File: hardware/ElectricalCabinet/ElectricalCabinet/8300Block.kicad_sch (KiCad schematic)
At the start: 0 parts

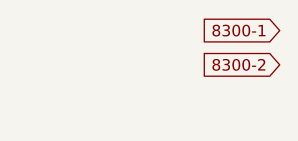
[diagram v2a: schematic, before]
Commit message: Further wiring updates
Populated 6100 Bus
Corrected number of relay boards
Added 110v outputs to relay boards and noted light positon
Uploaded light scheme to documents folder
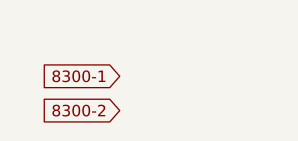
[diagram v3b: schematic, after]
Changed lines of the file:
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@@
 	(generator "eeschema")
 	(generator_version "10.0")
-	(paper "A4")
+	(paper "USLetter")
 	(global_label "8300-2"
 		(shape input)
-		(at 53.34 10.16 180)
+		(at 35.56 15.24 180)
 		(effects
 			(font
@@
 		)
 		(property "Intersheetrefs" "${INTERSHEET_REFS}"
-			(at 42.7349 10.16 0)
+			(at 24.9549 15.24 0)
 			(hide yes)
 			(show_name no)
@@
 		)
 		(property "Field" "5V Clock"
-			(at 44.45 10.16 0)
+			(at 26.67 15.24 0)
 			(hide yes)
 			(show_name no)
@@
 		)
 		(property "Ref" "Ref 333"
-			(at 43.18 10.16 0)
+			(at 25.4 15.24 0)
 			(show_name no)
 			(do_not_autoplace no)
@@
 	(global_label "8300-1"
 		(shape input)
-		(at 53.34 6.35 180)
+		(at 35.56 11.43 180)
 		(effects
 			(font
@@
 		)
 		(property "Intersheetrefs" "213"
-			(at 42.7349 6.35 0)
+			(at 24.9549 11.43 0)
 			(hide yes)
 			(show_name no)
@@
 		)
 		(property "Field" "5V Clock"
-			(at 44.45 6.35 0)
+			(at 26.67 11.43 0)
 			(hide yes)
 			(show_name no)
@@
 		)
 		(property "Ref" "Ref 213"
-			(at 43.18 6.35 0)
+			(at 25.4 11.43 0)
 			(show_name no)
 			(do_not_autoplace no)

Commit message: Electrical Cabinet done
Electrical Cabinet done, let me know if there are any changes or mistakes.
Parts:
- added U64, U65, U66, U67, U68, U69: (no value), symbol TrafficLightLibrary:Terminal_Block
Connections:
- net 8300-1: now also U64. (2)
- net 8300-2: now also U65. (2)
- new net: U64. (2), U65. (2), U66. (2), U67. (2), U68. (2), U69. (2)
- new net 8300-10: U66. (2)
- new net 8300-11: U65. (2)
- new net 8300-12: U64. (2)
- new net 8300-3: U66. (2)
- new net 8300-4: U67. (2)
- new net 8300-5: U68. (2)
- new net 8300-6: U69. (2)
- new net 8300-7: U69. (2)
- new net 8300-8: U68. (2)
- new net 8300-9: U67. (2)
